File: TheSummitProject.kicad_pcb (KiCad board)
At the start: 4 copper layers, 91.5 x 65 mm, 81 parts, among them IC1 STM32U5F7VJT6, J1 Cortex SWD, J4 Screen FPC, J5 Micro_SD_Card_Det1, Q1 NMOS, SW1 SW_SPDT, SW2 PWR_BTN, U1 NPM1300-CAAA-R, U2 USBLC6-2SC6, U3 USBLC6-2SC6, Y1 16Mhz, Y2 32.768Khz

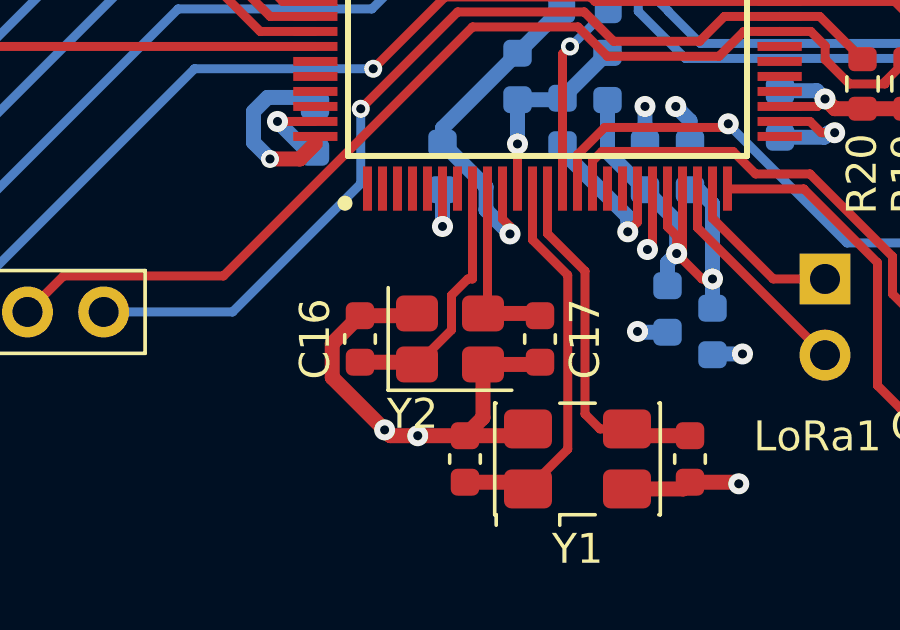
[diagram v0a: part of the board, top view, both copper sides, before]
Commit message: Updated footprint of 32.768k crystal to 3215
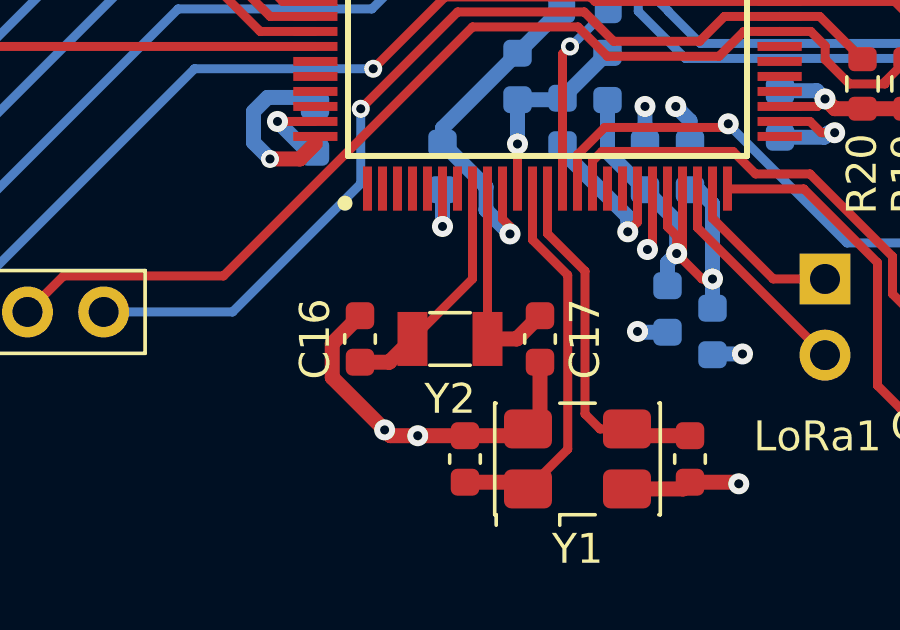
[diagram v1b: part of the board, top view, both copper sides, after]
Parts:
- Y2: footprint Crystal:Crystal_SMD_3225-4Pin_3.2x2.5mm -> Crystal:Crystal_SMD_3215-2Pin_3.2x1.5mm
- turned Y2 to 180 degrees
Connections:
- Y2 pad 2: GND -> Net-(IC1-LSE_OUT)
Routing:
- net GND: track 138.9 -> 135.1 mm
- net Net-(IC1-LSE_OUT): track 5.84 -> 7.08 mm
- net Net-(IC1-LSE_IN): track 8.54 -> 7.91 mm
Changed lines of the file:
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@@
 		(sheetname "/MCU/")
 		(sheetfile "TheSummitProject.kicad_sch")
+		(units
+			(unit
+				(name "A")
+				(pins "SH" "A1" "A12" "B1" "B12" "A4" "A9" "B4" "B9" "A5" "B5" "A7" "B7"
+					"A6" "B6"
+				)
+			)
+		)
 		(attr smd)
 		(duplicate_pad_numbers_are_jumpers no)
@@
 		(sheetname "/SD/")
 		(sheetfile "sd.kicad_sch")
+		(units
+			(unit
+				(name "A")
+				(pins "1" "2" "3" "4" "5" "6" "7" "8" "9" "SH")
+			)
+		)
 		(attr smd)
 		(duplicate_pad_numbers_are_jumpers no)
@@
 		)
 	)
-	(footprint "Crystal:Crystal_SMD_3225-4Pin_3.2x2.5mm"
+	(footprint "Crystal:Crystal_SMD_3215-2Pin_3.2x1.5mm"
 		(layer "F.Cu")
-		(at 140.974629 122.171934)
-		(descr "SMD3225/4, Crystal, 3.2x2.5mm package, SMD, http://www.txccrystal.com/images/pdf/7m-accuracy.pdf")
+		(at 140.974629 122.171934 180)
+		(descr "SMD Crystal FC-135 https://support.epson.biz/td/api/doc_check.php?dl=brief_FC-135R_en.pdf")
+		(tags "SMD SMT Crystal")
 		(property "Reference" "Y2"
-			(at -1.25 2.5 0)
+			(at 0 -2 0)
 			(layer "F.SilkS")
 			(effects
@@
 		)
 		(property "Value" "32.768Khz"
-			(at 0 2.45 0)
+			(at 0 2 0)
 			(layer "F.Fab")
 			(effects
@@
 		)
 		(property "Datasheet" ""
-			(at 0 0 0)
+			(at 0 0 180)
+			(unlocked yes)
 			(layer "F.Fab")
 			(hide yes)
@@
 				(font
 					(size 1.27 1.27)
+					(thickness 0.15)
 				)
 			)
 		)
-		(property "Description" "Four pin crystal, GND on pins 2 and 4"
-			(at 0 0 0)
+		(property "Description" ""
+			(at 0 0 180)
+			(unlocked yes)
 			(layer "F.Fab")
 			(hide yes)
@@
 				(font
 					(size 1.27 1.27)
-				)
-			)
-		)
-		(property "KiLib_Generator" "crystal_resonator_oscillator"
-			(at 0 0 0)
-			(layer "F.SilkS")
-			(hide yes)
-			(effects
-				(font
-					(size 1 1)
 					(thickness 0.15)
 				)
@@
 			(unit
 				(name "A")
-				(pins "1" "2" "4" "3")
+				(pins "1" "2")
 			)
 		)
@@
 		(duplicate_pad_numbers_are_jumpers no)
 		(fp_line
-			(start -2.06 -1.71)
-			(end -2.06 1.71)
+			(start -0.675 0.875)
+			(end 0.675 0.875)
 			(stroke
 				(width 0.12)
@@
 		)
 		(fp_line
-			(start -2.06 1.71)
-			(end 2.06 1.71)
+			(start -0.675 -0.875)
+			(end 0.675 -0.875)
 			(stroke
 				(width 0.12)
@@
 			(layer "F.SilkS")
 		)
-		(fp_rect
-			(start -2.1 -1.75)
-			(end 2.1 1.75)
+		(fp_line
+			(start 2 -1.15)
+			(end 2 1.15)
 			(stroke
 				(width 0.05)
 				(type solid)
 			)
-			(fill no)
 			(layer "F.CrtYd")
 		)
-		(fp_poly
-			(pts
-				(xy 1.6 -1.25) (xy 1.6 1.25) (xy -0.975 1.25) (xy -1.6 0.625) (xy -1.6 -1.25)
+		(fp_line
+			(start -2 1.15)
+			(end 2 1.15)
+			(stroke
+				(width 0.05)
+				(type solid)
 			)
+			(layer "F.CrtYd")
+		)
+		(fp_line
+			(start -2 -1.15)
+			(end 2 -1.15)
+			(stroke
+				(width 0.05)
+				(type solid)
+			)
+			(layer "F.CrtYd")
+		)
+		(fp_line
+			(start -2 -1.15)
+			(end -2 1.15)
+			(stroke
+				(width 0.05)
+				(type solid)
+			)
+			(layer "F.CrtYd")
+		)
+		(fp_line
+			(start 1.6 -0.75)
+			(end 1.6 0.75)
+			(stroke
+				(width 0.1)
+				(type solid)
+			)
+			(layer "F.Fab")
+		)
+		(fp_line
+			(start -1.6 0.75)
+			(end 1.6 0.75)
+			(stroke
+				(width 0.1)
+				(type solid)
+			)
+			(layer "F.Fab")
+		)
+		(fp_line
+			(start -1.6 -0.75)
+			(end 1.6 -0.75)
+			(stroke
+				(width 0.1)
+				(type solid)
+			)
+			(layer "F.Fab")
+		)
+		(fp_line
+			(start -1.6 -0.75)
+			(end -1.6 0.75)
 			(stroke
 				(width 0.1)
 				(type solid)
 			)
-			(fill no)
 			(layer "F.Fab")
 		)
 		(fp_text user "${REFERENCE}"
-			(at 0 0 0)
+			(at 0 -2 0)
 			(layer "F.Fab")
 			(effects
 				(font
-					(size 0.8 0.8)
-					(thickness 0.12)
+					(size 1 1)
+					(thickness 0.15)
 				)
 			)
 		)
-		(pad "1" smd roundrect
-			(at -1.1 0.85)
-			(size 1.4 1.2)
+		(pad "1" smd rect
+			(at 1.25 0 180)
+			(size 1 1.8)
 			(layers "F.Cu" "F.Mask" "F.Paste")
-			(roundrect_rratio 0.208333)
 			(net "Net-(IC1-LSE_IN)")
 			(pinfunction "1_1")
 			(pintype "passive")
 		)
-		(pad "2" smd roundrect
-			(at 1.1 0.85)
-			(size 1.4 1.2)
-			(layers "F.Cu" "F.Mask" "F.Paste")
-			(roundrect_rratio 0.208333)
-			(net "GND")
-			(pinfunction "G_2")
-			(pintype "passive")
-		)
-		(pad "3" smd roundrect
-			(at 1.1 -0.85)
-			(size 1.4 1.2)
+		(pad "2" smd rect
+			(at -1.25 0 180)
+			(size 1 1.8)
 			(layers "F.Cu" "F.Mask" "F.Paste")
-			(roundrect_rratio 0.208333)
 			(net "Net-(IC1-LSE_OUT)")
-			(pinfunction "3_3")
-			(pintype "passive")
-		)
-		(pad "4" smd roundrect
-			(at -1.1 -0.85)
-			(size 1.4 1.2)
-			(layers "F.Cu" "F.Mask" "F.Paste")
-			(roundrect_rratio 0.208333)
-			(net "GND")
-			(pinfunction "G_4")
+			(pinfunction "2_2")
 			(pintype "passive")
 		)
 		(embedded_fonts no)
-		(model "${KICAD10_3DMODEL_DIR}/Crystal.3dshapes/Crystal_SMD_3225-4Pin_3.2x2.5mm.step"
+		(model "${KICAD10_3DMODEL_DIR}/Crystal.3dshapes/Crystal_SMD_3215-2Pin_3.2x1.5mm.step"
 			(offset
 				(xyz 0 0 0)
@@
 	)
 	(segment
+		(start 143.974629 122.946934)
+		(end 143.974629 124.771934)
+		(width 0.5)
+		(layer "F.Cu")
+		(net "GND")
+	)
+	(segment
 		(start 153.349624 115.296929)
 		(end 153.796531 115.296929)
@@
 	)
 	(segment
+		(start 143.974629 124.771934)
+		(end 143.574629 125.171934)
+		(width 0.5)
+		(layer "F.Cu")
+		(net "GND")
+	)
+	(segment
 		(start 175.758786 102.491214)
 		(end 177 101.25)
@@
 	)
 	(segment
-		(start 142.074629 123.021934)
-		(end 143.899629 123.021934)
-		(width 0.5)
-		(layer "F.Cu")
-		(net "GND")
-	)
-	(segment
 		(start 175.731786 103.301635)
 		(end 175.685787 103.347634)
@@
 	)
 	(segment
-		(start 142.074629 123.021934)
-		(end 142.074629 124.796934)
-		(width 0.5)
-		(layer "F.Cu")
-		(net "GND")
-	)
-	(segment
 		(start 185.210786 96.910786)
 		(end 185.2 96.9)
@@
 	)
 	(segment
-		(start 142.074629 124.796934)
-		(end 141.474629 125.396934)
-		(width 0.5)
-		(layer "F.Cu")
-		(net "GND")
-	)
-	(segment
 		(start 136.486629 114.921934)
 		(end 135.224629 114.921934)
@@
 	)
 	(segment
-		(start 137.974629 121.396934)
-		(end 139.799629 121.396934)
-		(width 0.5)
-		(layer "F.Cu")
-		(net "GND")
-	)
-	(segment
 		(start 178.685786 98.496234)
 		(end 178.685786 99.814214)
@@
 	)
 	(segment
-		(start 141.024629 121.871934)
-		(end 141.024629 120.716478)
-		(width 0.3)
+		(start 137.974629 122.946934)
+		(end 138.949629 122.946934)
+		(width 0.5)
 		(layer "F.Cu")
 		(net "Net-(IC1-LSE_IN)")
 	)
 	(segment
-		(start 141.569173 120.171934)
+		(start 141.724629 117.159934)
 		(end 141.724629 120.171934)
 		(width 0.3)
@@
 	)
 	(segment
-		(start 141.024629 120.716478)
-		(end 141.569173 120.171934)
-		(width 0.3)
-		(layer "F.Cu")
-		(net "Net-(IC1-LSE_IN)")
-	)
-	(segment
-		(start 137.974629 122.946934)
-		(end 139.799629 122.946934)
+		(start 138.949629 122.946934)
+		(end 139.724629 122.171934)
 		(width 0.5)
 		(layer "F.Cu")
@@
 	)
 	(segment
-		(start 139.874629 123.021934)
-		(end 141.024629 121.871934)
-		(width 0.3)
-		(layer "F.Cu")
-		(net "Net-(IC1-LSE_IN)")
-	)
-	(segment
 		(start 141.724629 120.171934)
-		(end 141.724629 117.159934)
+		(end 139.724629 122.171934)
 		(width 0.3)
 		(layer "F.Cu")
@@
 	)
 	(segment
-		(start 142.074629 121.321934)
-		(end 143.899629 121.321934)
+		(start 142.224629 117.159934)
+		(end 142.224629 122.171934)
+		(width 0.3)
+		(layer "F.Cu")
+		(net "Net-(IC1-LSE_OUT)")
+	)
+	(segment
+		(start 142.224629 122.171934)
+		(end 143.199629 122.171934)
 		(width 0.5)
 		(layer "F.Cu")
@@
 	)
 	(segment
-		(start 142.224629 121.171934)
-		(end 142.224629 117.159934)
-		(width 0.3)
+		(start 143.199629 122.171934)
+		(end 143.974629 121.396934)
+		(width 0.5)
 		(layer "F.Cu")
 		(net "Net-(IC1-LSE_OUT)")

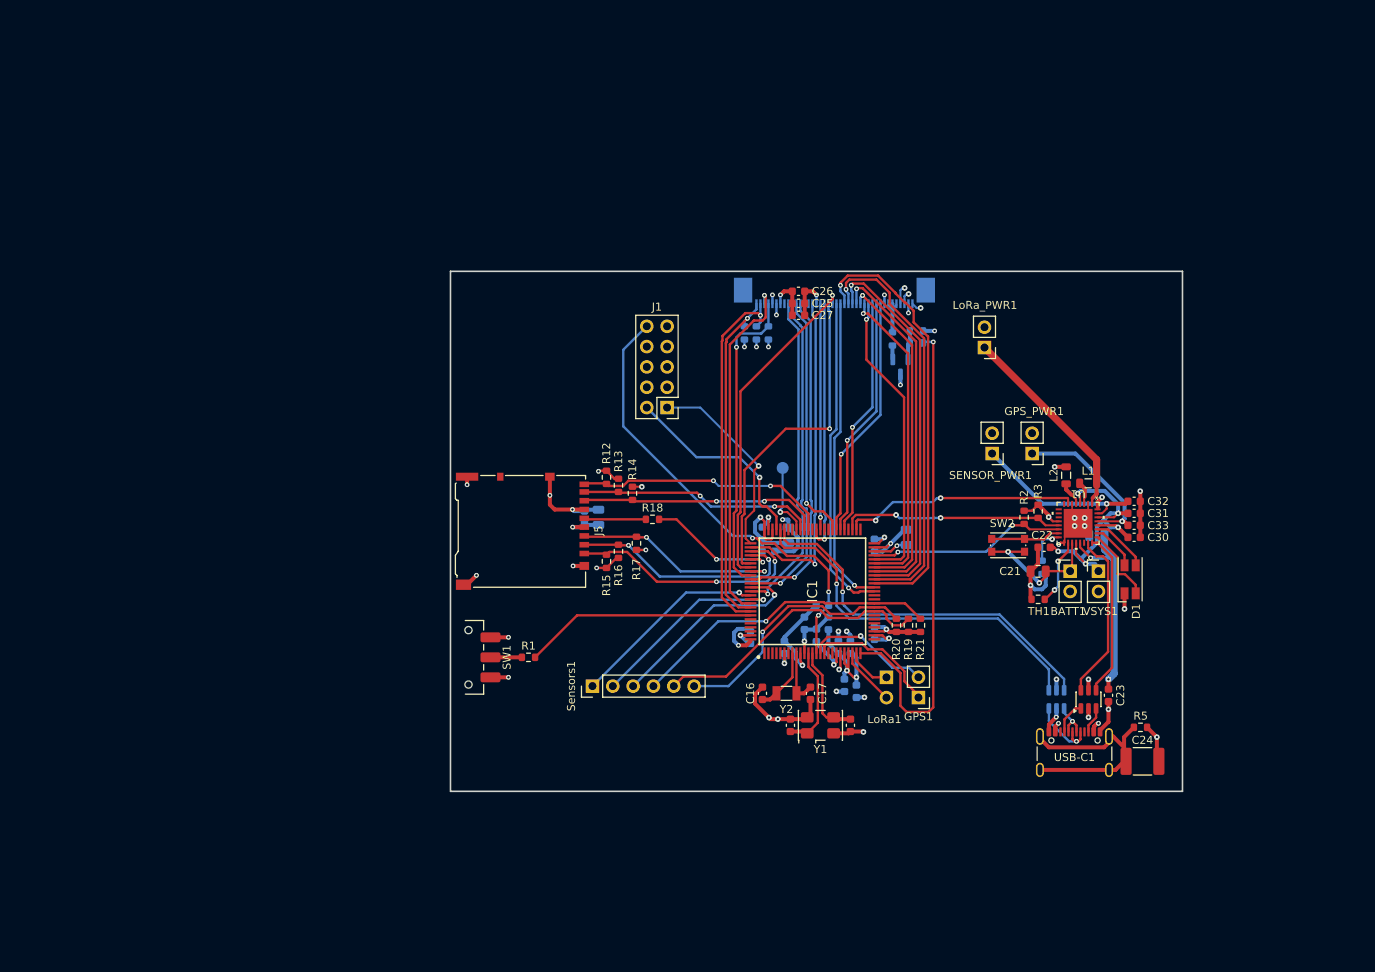
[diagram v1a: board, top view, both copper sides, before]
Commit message: added mux for usb, cleaned up schematic for pcb design, setup new pcb with correct size
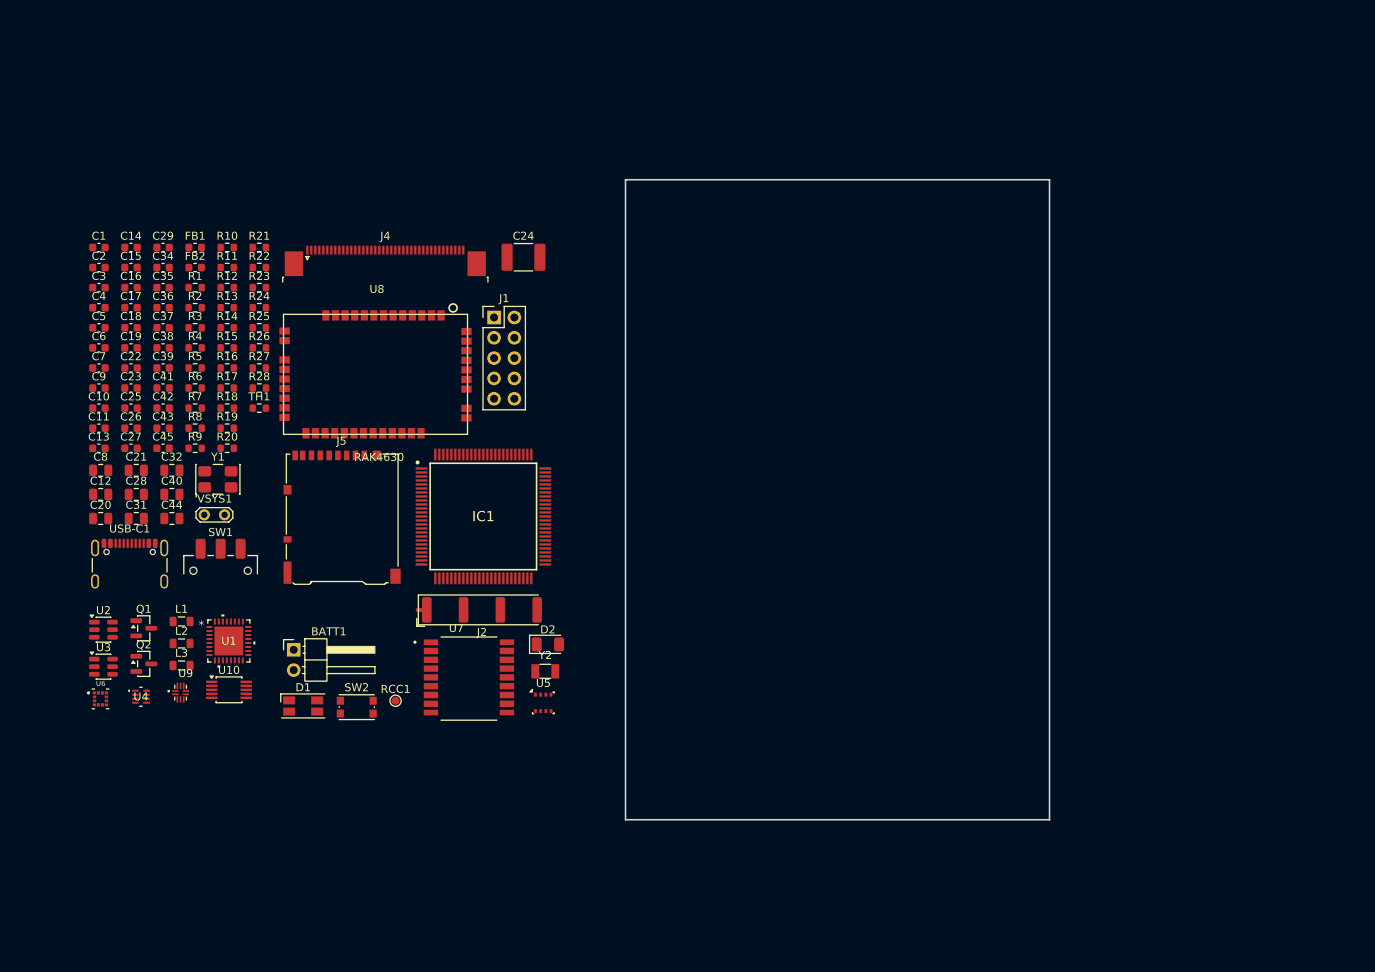
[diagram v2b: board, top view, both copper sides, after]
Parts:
- removed C30: 1u, Capacitor_SMD:C_0603_1608Metric
- removed C33: 2.2u, Capacitor_SMD:C_0603_1608Metric
- removed GPS1: GPS, Connector_PinHeader_2.54mm:PinHeader_1x02_P2.54mm_Vertical
- removed GPS_PWR1: GPS PWR, Connector_PinHeader_2.54mm:PinHeader_1x02_P2.54mm_Vertical
- removed LoRa1: LoRa, Connector_PinHeader_2.54mm:PinHeader_1x02_P2.54mm_Vertical
- removed LoRa_PWR1: 3.3v LORA, Connector_PinHeader_2.54mm:PinHeader_1x02_P2.54mm_Vertical
- removed SENSOR_PWR1: Sensor PWR, Connector_PinHeader_2.54mm:PinHeader_1x02_P2.54mm_Vertical
- removed Sensors1: Sensors, Connector_PinHeader_2.54mm:PinHeader_1x06_P2.54mm_Vertical
- added C34: 220n, Capacitor_SMD:C_0603_1608Metric, F.Cu at (63.1, 69.0)
- added C35: 100n, Capacitor_SMD:C_0603_1608Metric, F.Cu at (63.1, 71.5)
- added C36: 100n, Capacitor_SMD:C_0603_1608Metric, F.Cu at (63.1, 74.0)
- added C37: 100n, Capacitor_SMD:C_0603_1608Metric, F.Cu at (63.1, 76.5)
- added C38: 100n, Capacitor_SMD:C_0603_1608Metric, F.Cu at (63.1, 79.0)
- added C39: 100n, Capacitor_SMD:C_0603_1608Metric, F.Cu at (63.1, 81.5)
- added C40: 10u, Capacitor_SMD:C_0805_2012Metric, F.Cu at (64.2, 97.3)
- added C41: 100n, Capacitor_SMD:C_0603_1608Metric, F.Cu at (63.1, 84.0)
- added C42: 100n, Capacitor_SMD:C_0603_1608Metric, F.Cu at (63.1, 86.5)
- added C43: 100n, Capacitor_SMD:C_0603_1608Metric, F.Cu at (63.1, 89.0)
- added C44: 10u, Capacitor_SMD:C_0805_2012Metric, F.Cu at (64.2, 100.3)
- added C45: 100n, Capacitor_SMD:C_0603_1608Metric, F.Cu at (63.1, 91.5)
- added D2: Blue_LED, LED_SMD:LED_1206_3216Metric, F.Cu at (111.2, 116.0)
- added FB2: 100R, Inductor_SMD:L_0603_1608Metric, F.Cu at (67.1, 69.0)
- added J2: GPS_ANT, RF_Antenna:Antenova_SR4G013_GPS, F.Cu at (102.9, 111.7)
- added L3: 2.2u, Inductor_SMD:L_0805_2012Metric, F.Cu at (65.4, 118.7)
- added Q2: PMOS, Package_TO_SOT_SMD:SOT-23, F.Cu at (60.6, 118.5)
- added R22: 100k, Resistor_SMD:R_0603_1608Metric, F.Cu at (75.1, 69.0)
- added R23: 100k, Resistor_SMD:R_0603_1608Metric, F.Cu at (75.1, 71.5)
- added R24: 100k, Resistor_SMD:R_0603_1608Metric, F.Cu at (75.1, 74.0)
- added R25: 10k, Resistor_SMD:R_0603_1608Metric, F.Cu at (75.1, 76.5)
- added R26: 100k, Resistor_SMD:R_0603_1608Metric, F.Cu at (75.1, 79.0)
- added R27: 100k, Resistor_SMD:R_0603_1608Metric, F.Cu at (75.1, 81.5)
- added R28: 100, Resistor_SMD:R_0603_1608Metric, F.Cu at (75.1, 84.0)
- added U10: TS3USB30EDGSR, Package_SO:TSSOP-10_3x3mm_P0.5mm, F.Cu at (71.3, 121.7)
- added U4: TPS62840DLCR, TheSummitProject:VSON8_2P1X1P6_TEX, F.Cu at (60.3, 122.6)
- added U5: BME280, Package_LGA:Bosch_LGA-8_2.5x2.5mm_P0.65mm_ClockwisePinNumbering, F.Cu at (110.6, 123.4)
- added U6: LSM303AGR, TheSummitProject:PQFN50P200X200X100-12N, F.Cu at (55.2, 122.9)
- added U7: MAX-M10S-00B, TheSummitProject:XCVR_MAX-M10S-00B, F.Cu at (101.3, 120.2)
- added U8: RAK4630, TheSummitProject:RAK4630, F.Cu at (89.6, 82.3)
- added U9: SN74AVC2T245RSWR, TheSummitProject:QFN40P180X140X55-10N, F.Cu at (65.2, 122.1)
- BATT1: footprint Connector_PinHeader_2.54mm:PinHeader_1x02_P2.54mm_Vertical -> Connector_PinHeader_2.54mm:PinHeader_1x02_P2.54mm_Horizontal
- C1, C10, C11, C12, C13, C18, C19, C2, C20, C28, C3, C4, C5, C6, C7, C8, C9, FB1, J4, Q1, R10, R11, R6, R7, R8, R9, U3: moved to F.Cu
- C25, C26: value 0.1u -> 100n
- C29: value 0.1u -> 100n; moved to F.Cu
- C31: value 1u -> 4.7u; footprint Capacitor_SMD:C_0603_1608Metric -> Capacitor_SMD:C_0805_2012Metric
- C32: value 2.2u -> 10u; footprint Capacitor_SMD:C_0603_1608Metric -> Capacitor_SMD:C_0805_2012Metric
- R4: value 350k -> 47k; moved to F.Cu
- RCC1: footprint TestPoint:TestPoint_Pad_D1.5mm -> TestPoint:TestPoint_Pad_D1.0mm; moved to F.Cu
- VSYS1: footprint Connector_PinHeader_2.54mm:PinHeader_1x02_P2.54mm_Vertical -> TestPoint:TestPoint_2Pads_Pitch2.54mm_Drill0.8mm
- moved C23 128.1 mm to (59.0, 84.0), turned to 0 degrees
- moved R5 126.4 mm to (67.1, 81.5), turned to 0 degrees
- moved C31 124.7 mm to (59.7, 100.3), turned to 0 degrees
- moved C20 124.5 mm to (55.3, 100.3)
- moved U2 123.4 mm to (55.6, 114.2), turned to 0 degrees
- moved USB-C1 120.4 mm to (58.9, 107.1)
- moved C32 120.3 mm to (64.2, 94.3), turned to 0 degrees
- moved U3 119.2 mm to (55.6, 118.8), turned to 0 degrees
- moved C22 116.3 mm to (59.0, 81.5), turned to 0 degrees
- moved L1 114.6 mm to (65.4, 113.2)
- moved C21 113.4 mm to (59.7, 94.3)
- moved L2 112.6 mm to (65.4, 115.9), turned to 0 degrees
- moved VSYS1 112.0 mm to (68.2, 99.9)
- moved R4 109.4 mm to (67.1, 79.0), turned to 0 degrees
- moved C14 108.0 mm to (59.0, 66.4), turned to 0 degrees
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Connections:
- net +3.3VA renamed +1.8VA
- BATT1 pad 1: VBAT -> Net-(BATT1-Pin_1)
- C1 pad 1: +3.3V -> +1.8V
- C11 pad 1: +3.3V -> +1.8V
- C2 pad 1: +3.3V -> +1.8V
- C25 pad 1: +3.3V_DP_LORA -> +1.8V
- C26 pad 2: +3.3V_DP_LORA -> +1.8V
- C27 pad 1: +3.3V_DP_LORA -> +1.8V
- C28 pad 2: +3.3V -> +3.3V_HP
- C29 pad 2: +3.3V -> +3.3V_HP
- C3 pad 1: +3.3V -> +1.8V
- C32 pad 1: GND -> +3.3V_HP
- C32 pad 2: LSOUT2 -> GND
- C4 pad 1: +3.3V -> +1.8V
- C5 pad 1: +3.3V -> +1.8V
- C6 pad 1: +3.3V -> +1.8V
- C7 pad 1: +3.3V -> +1.8V
- C8 pad 1: +3.3V -> +1.8V
- FB1 pad 2: +3.3V -> +1.8V
- IC1 pad 100: +3.3V -> +1.8V
- IC1 pad 11: +3.3V -> +1.8V
- IC1 pad 15: GPS_TX -> GPS_RX
- IC1 pad 16: GPS_RX -> GPS_TX
- IC1 pad 17: unconnected-(IC1-PC2-Pad17) -> GPS_INT
- IC1 pad 28: +3.3V -> +1.8V
- IC1 pad 50: +3.3V -> +1.8V
- IC1 pad 6: +3.3V -> +1.8V
- IC1 pad 69: unconnected-(IC1-PA10-Pad69) -> Net-(IC1-PA10)
- IC1 pad 75: +3.3V -> +1.8V
- J1 pad 4: +3.3V -> +1.8V
- J1 pad 7: +3.3V -> +1.8V
- J4 pad 33: +3.3V_DP_LORA -> +3.3V_HP
- J4 pad 39: +3.3V_DP_LORA -> +1.8V
- J4 pad 6: +3.3V_DP_LORA -> +1.8V
- J4 pad 7: +3.3V_DP_LORA -> +1.8V
- J5 pad 4: +3.3V -> +3.3V_HP
- L1 pad 2: +3.3V_DP_LORA -> +1.8V
- R12 pad 1: +3.3V -> +3.3V_HP
- R13 pad 1: +3.3V -> +3.3V_HP
- R14 pad 1: +3.3V -> +3.3V_HP
- R15 pad 2: +3.3V -> +3.3V_HP
- R16 pad 2: +3.3V -> +3.3V_HP
- R17 pad 2: +3.3V -> +3.3V_HP
- R19 pad 1: +3.3V -> +1.8V
- R2 pad 2: +3.3V -> +1.8V
- R20 pad 1: +3.3V -> +1.8V
- R21 pad 1: +3.3V -> +1.8V
- R3 pad 2: +3.3V -> +1.8V
- R4 pad 1: Net-(U1-VSET2) -> GND
- R4 pad 2: GND -> Net-(U1-VSET1)
- R6 pad 2: +3.3V_DP_LORA -> +1.8V
- R7 pad 2: +3.3V_DP_LORA -> +1.8V
- R8 pad 2: +3.3V_DP_LORA -> +1.8V
- SW1 pad 3: +3.3V -> +1.8V
- U1 pad 1: +3.3V_DP_LORA -> +1.8V
- U1 pad 12: +3.3V -> +1.8V
- U1 pad 16: Net-(U1-VSET2) -> GND
- U1 pad 17: GND -> Net-(U1-VSET1)
- U1 pad 28: VSYS -> unconnected-(U1-LSIN1/VINLDO1-Pad28)
- U1 pad 29: LSOUT1 -> unconnected-(U1-LSOUT1/VOUTLDO1-Pad29)
- U1 pad 30: VSYS -> unconnected-(U1-LSIN2/VINLDO2-Pad30)
- U1 pad 31: LSOUT2 -> unconnected-(U1-LSOUT2/VOUTLDO2-Pad31)
- U3 pad 4: Net-(IC1-USB_OTG_HS_DP) -> Net-(U10-D-)
- U3 pad 6: Net-(IC1-USB_OTG_HS_DM) -> Net-(U10-D+)
- USB-C1 pad A6: Net-(U3-I/O2-Pad3) -> Net-(U3-I/O1-Pad1)
- USB-C1 pad A7: Net-(U3-I/O1-Pad1) -> Net-(U3-I/O2-Pad3)
- USB-C1 pad B6: Net-(U3-I/O2-Pad3) -> Net-(U3-I/O1-Pad1)
- USB-C1 pad B7: Net-(U3-I/O1-Pad1) -> Net-(U3-I/O2-Pad3)
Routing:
- net GND: track 135.1 -> 0.00 mm, vias 39 -> 0
- net +3.3V: track 64.4 -> 0.00 mm, vias 16 -> 0
- net LCD_PWM: track 61.6 -> 0.00 mm, vias 1 -> 0
- net /MCU/NRST: track 57.8 -> 0.00 mm, vias 3 -> 0
- net LCD_D6: track 54.6 -> 0.00 mm, vias 1 -> 0
- net LCD_D7: track 51.9 -> 0.00 mm, vias 1 -> 0
- net LCD_D8: track 48.3 -> 0.00 mm, vias 1 -> 0
- net Net-(IC1-USB_OTG_HS_DM): track 47.4 -> 0.00 mm, vias 1 -> 0
- net Net-(IC1-USB_OTG_HS_DP): track 47.1 -> 0.00 mm, vias 1 -> 0
- net CTP_SDA: track 46.1 -> 0.00 mm, vias 1 -> 0
- net LCD_D9: track 45.4 -> 0.00 mm, vias 1 -> 0
- net CTP_RST: track 43.8 -> 0.00 mm, vias 1 -> 0
- net CTP_SCL: track 42.9 -> 0.00 mm, vias 1 -> 0
- net LCD_D10: track 41.9 -> 0.00 mm, vias 1 -> 0
- net LCD_RST: track 41.7 -> 0.00 mm, vias 1 -> 0
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- removed copper zone on In2.Cu, net +3.3V
- removed copper zone on In2.Cu, net +3.3V_DP_LORA
- removed copper zone on In1.Cu, net GND
- removed copper zone on In2.Cu, net VBUS
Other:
- board size 91.5 x 65 mm -> 53 x 80 mm
- copper layers 4 -> 2

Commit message: changed FB2 to 120R to consilidate BOM
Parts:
- FB2: value 100R -> 120R
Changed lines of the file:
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@@
 			)
 		)
-		(property "Value" "100R"
+		(property "Value" "120R"
 			(at 0 1.43 0)
 			(layer "F.Fab")
